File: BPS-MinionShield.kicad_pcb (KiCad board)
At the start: 2 copper layers, 85 x 66 mm, 81 parts, among them J1 TempConn1, J2 TempConn2, J3 Conn_01x24_Female

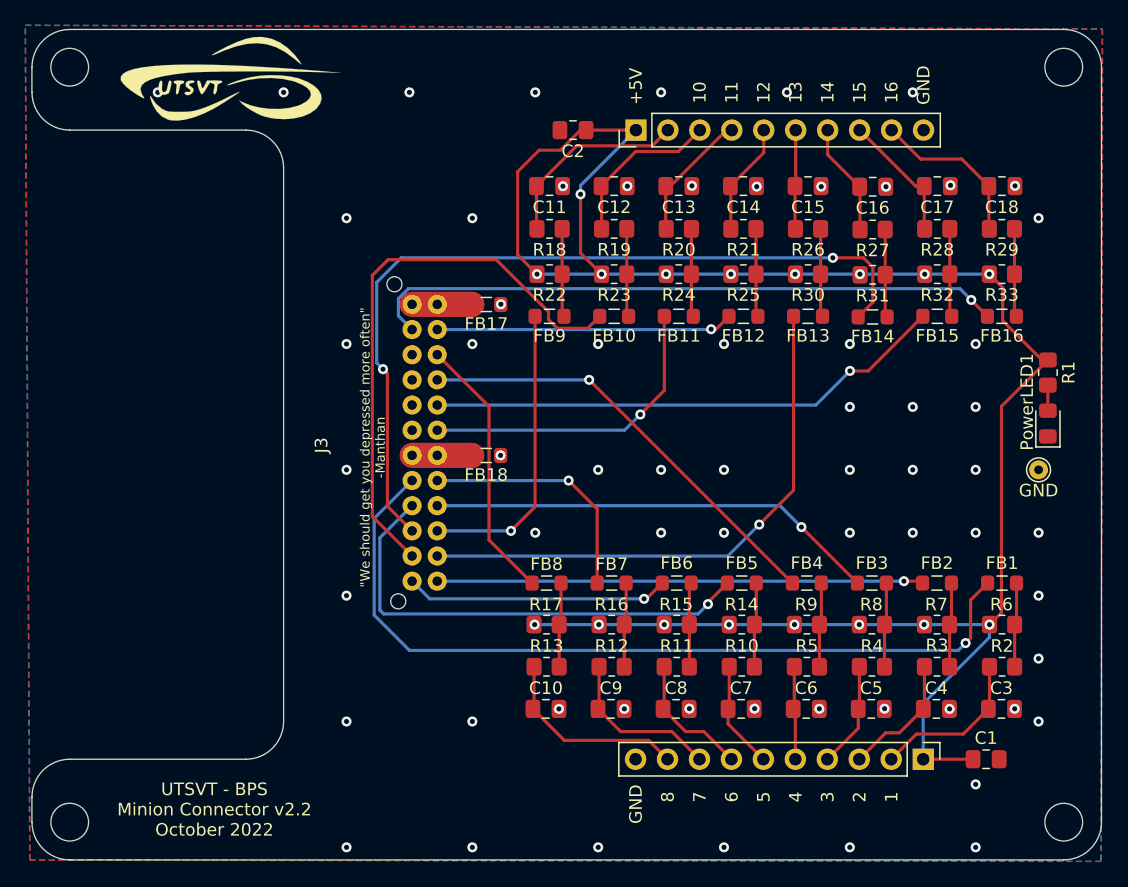
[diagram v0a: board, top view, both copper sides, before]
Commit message: move ferrite beads away from connector
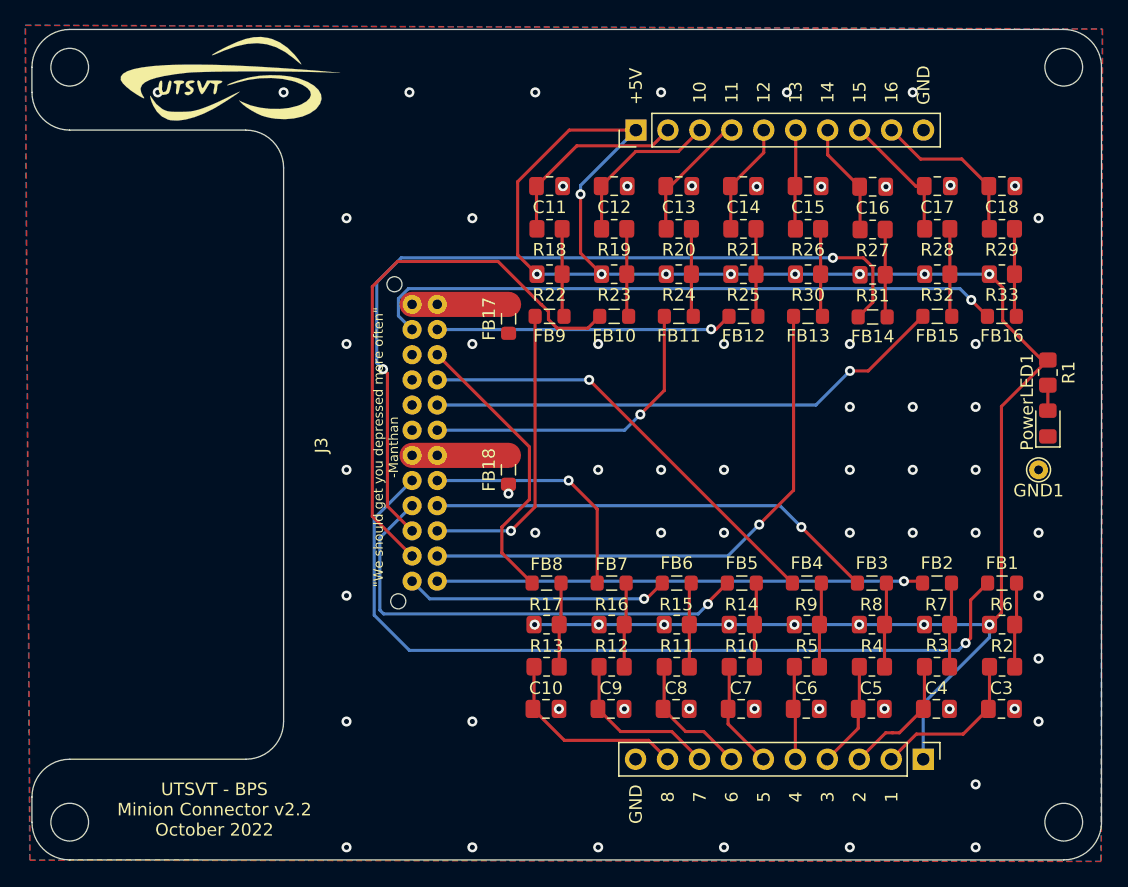
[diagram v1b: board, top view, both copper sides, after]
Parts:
- removed C1, C2: 1u, Capacitor_SMD:C_0805_2012Metric_Pad1.18x1.45mm_HandSolder
- moved FB18 2.11 mm to (137.9, 105.0), turned to 90 degrees
- moved FB17 2.11 mm to (137.9, 93.0), turned to 90 degrees
- renumbered GND to GND1
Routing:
- net +5V: track 154.4 -> 150.0 mm
- net Net-(FB18-Pad2): track 4.74 -> 7.66 mm
- net Net-(FB17-Pad2): track 4.75 -> 7.67 mm
- net /temp14: track 21.3 -> 23.1 mm
- net /temp7: track 45.2 -> 44.6 mm
- net GND: vias 64 -> 63

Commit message: fix some islands
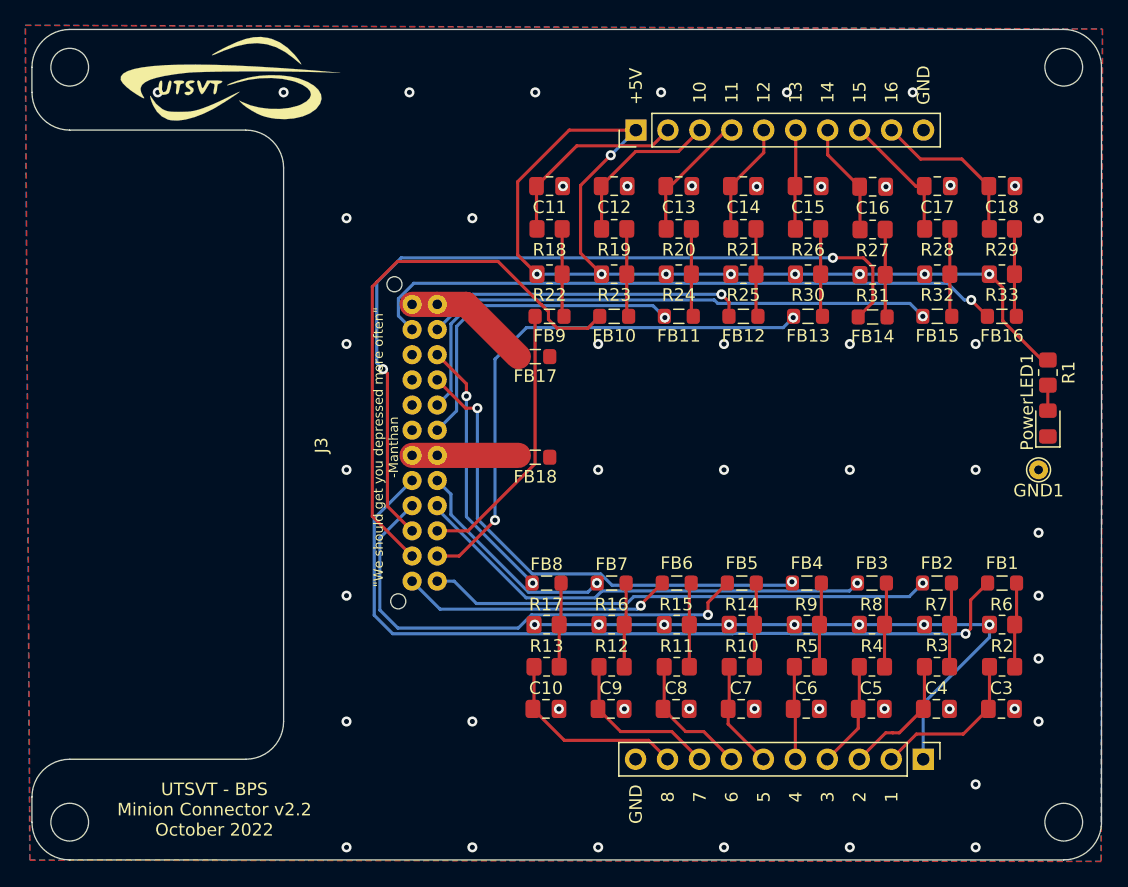
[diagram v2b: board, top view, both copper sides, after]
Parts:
- moved FB17 3.67 mm to (140.0, 96.0), turned to 180 degrees
- moved FB18 2.35 mm to (140.0, 104.0), turned to 180 degrees
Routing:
- net +5V: track 150.0 -> 127.1 mm
- net /temp13: track 34.9 -> 40.2 mm, vias 1 -> 2
- net /temp12: track 41.5 -> 45.7 mm
- net Net-(FB17-Pad2): track 7.67 -> 10.2 mm
- net /temp15: track 23.6 -> 25.7 mm
- net /temp3: track 23.7 -> 21.7 mm, vias 1 -> 0
- net /temp10: track 19.5 -> 17.6 mm
- net /temp14: track 23.1 -> 21.3 mm, vias 0 -> 2
- net /temp1: track 65.8 -> 64.3 mm
- net /temp2: track 38.2 -> 39.6 mm
- net /temp5: track 38.6 -> 40.0 mm
- net /temp11: track 25.2 -> 26.5 mm
- net /temp9: track 35.9 -> 37.1 mm
- net Net-(FB18-Pad2): track 7.66 -> 8.45 mm
- net /temp6: track 21.0 -> 21.7 mm
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
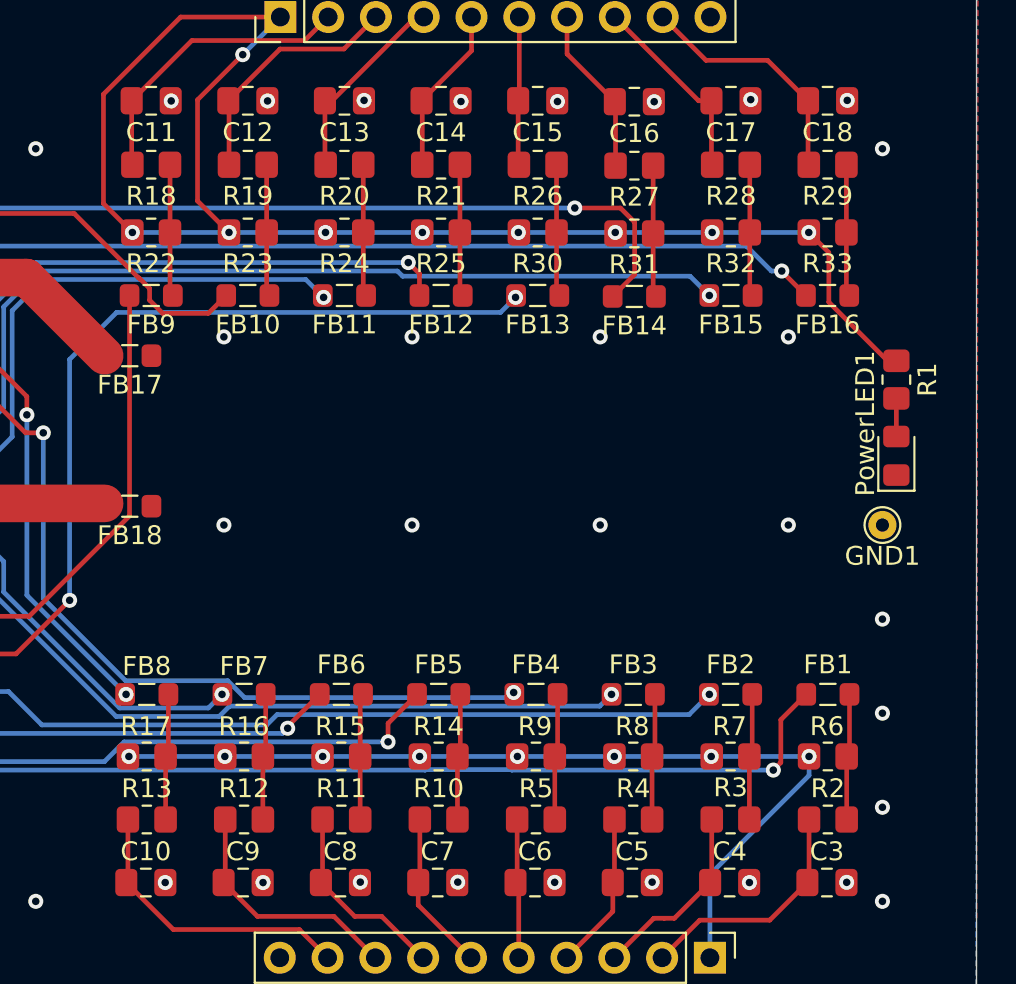
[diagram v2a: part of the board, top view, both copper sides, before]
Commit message: change cap values to 100nf
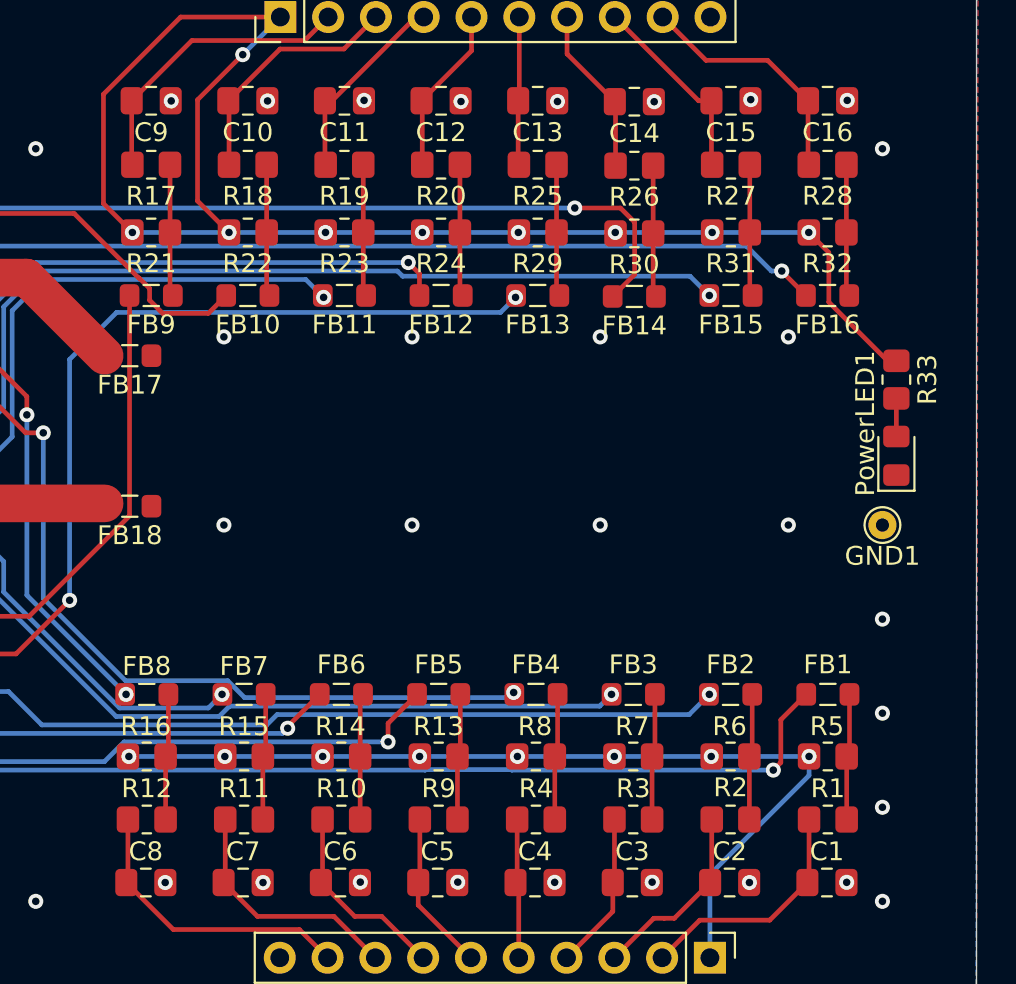
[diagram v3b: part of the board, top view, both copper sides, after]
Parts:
- C1: renamed from C3; value 1u -> 100nF
- C10: renamed from C12; value 1u -> 100nF
- C11: renamed from C13; value 1u -> 100nF
- C12: renamed from C14; value 1u -> 100nF
- C13: renamed from C15; value 1u -> 100nF
- C14: renamed from C16; value 1u -> 100nF
- C15: renamed from C17; value 1u -> 100nF
- C16: renamed from C18; value 1u -> 100nF
- C2: renamed from C4; value 1u -> 100nF
- C3: renamed from C5; value 1u -> 100nF
- C4: renamed from C6; value 1u -> 100nF
- C5: renamed from C7; value 1u -> 100nF
- C6: renamed from C8; value 1u -> 100nF
- C7: renamed from C9; value 1u -> 100nF
- C8: renamed from C10; value 1u -> 100nF
- C9: renamed from C11; value 1u -> 100nF
- renumbered R2 to R1, R11 to R10, R12 to R11, R13 to R12, R14 to R13, R15 to R14, R16 to R15, R17 to R16, R18 to R17, R19 to R18, R20 to R19, R3 to R2, R21 to R20, R22 to R21, R23 to R22, R24 to R23, R25 to R24, R26 to R25, R27 to R26, R28 to R27, R29 to R28, R30 to R29, R4 to R3, R31 to R30, R32 to R31, R33 to R32, R1 to R33, R5 to R4, R6 to R5, R7 to R6, R8 to R7, R9 to R8, R10 to R9

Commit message: address maestro tianda's review
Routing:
- net +5V: track 127.1 -> 112.8 mm, vias 17 -> 16
- net /temp1: track 64.3 -> 64.9 mm
- net /temp2: track 39.6 -> 39.1 mm
- net GND: vias 50 -> 39
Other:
- board text added: "9"

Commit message: address all tianda requests, start standardization
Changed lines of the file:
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@@
   (segment (start 152.407144 89.45) (end 152.407144 92.65) (width 0.25) (layer "F.Cu") (net 39))
   (segment (start 152.407144 85.85) (end 152.407144 89.45) (width 0.25) (layer "F.Cu") (net 39))
-  (via (at 150.3 92.9) (size 0.8) (drill 0.4) (layers "F.Cu" "B.Cu") (net 40))
-  (segment (start 133.747 93.603) (end 135.4 91.95) (width 0.25) (layer "B.Cu") (net 40))
-  (segment (start 132.21 101.85) (end 133.747 100.313) (width 0.25) (layer "B.Cu") (net 40))
-  (segment (start 149.35 91.95) (end 150.3 92.9) (width 0.25) (layer "B.Cu") (net 40))
-  (segment (start 135.4 91.95) (end 149.35 91.95) (width 0.25) (layer "B.Cu") (net 40))
-  (segment (start 133.747 100.313) (end 133.747 93.603) (width 0.25) (layer "B.Cu") (net 40))
+  (via (at 150.257144 92.8) (size 0.8) (drill 0.4) (layers "F.Cu" "B.Cu") (net 40))
+  (segment (start 149.407144 91.95) (end 135.4 91.95) (width 0.25) (layer "B.Cu") (net 40))
+  (segment (start 150.257144 92.8) (end 149.407144 91.95) (width 0.25) (layer "B.Cu") (net 40))
+  (segment (start 133.747 93.603) (end 133.747 100.313) (width 0.25) (layer "B.Cu") (net 40))
+  (segment (start 133.747 100.313) (end 132.21 101.85) (width 0.25) (layer "B.Cu") (net 40))
+  (segment (start 135.4 91.95) (end 133.747 93.603) (width 0.25) (layer "B.Cu") (net 40))
   (segment (start 157.542858 85.85) (end 157.542858 89.45) (width 0.25) (layer "F.Cu") (net 41))
   (segment (start 157.542858 92.65) (end 157.692858 92.8) (width 0.25) (layer "F.Cu") (net 41))
@@
   (segment (start 133.95 111.85) (end 132.21 111.85) (width 0.25) (layer "F.Cu") (net 44))
   (segment (start 136.8 109) (end 133.95 111.85) (width 0.25) (layer "F.Cu") (net 44))
-  (via (at 160.5 92.9) (size 0.8) (drill 0.4) (layers "F.Cu" "B.Cu") (net 44))
+  (via (at 160.528572 92.8) (size 0.8) (drill 0.4) (layers "F.Cu" "B.Cu") (net 44))
   (via (at 136.8 109) (size 0.8) (drill 0.4) (layers "F.Cu" "B.Cu") (net 44))
-  (segment (start 139.3 93.7) (end 159.7 93.7) (width 0.25) (layer "B.Cu") (net 44))
-  (segment (start 136.8 109) (end 136.8 96.2) (width 0.25) (layer "B.Cu") (net 44))
-  (segment (start 136.8 96.2) (end 139.3 93.7) (width 0.25) (layer "B.Cu") (net 44))
-  (segment (start 159.7 93.7) (end 160.5 92.9) (width 0.25) (layer "B.Cu") (net 44))
+  (segment (start 159.788572 93.54) (end 139.46 93.54) (width 0.25) (layer "B.Cu") (net 44))
+  (segment (start 136.8 96.2) (end 136.8 109) (width 0.25) (layer "B.Cu") (net 44))
+  (segment (start 160.528572 92.8) (end 159.788572 93.54) (width 0.25) (layer "B.Cu") (net 44))
+  (segment (start 139.46 93.54) (end 136.8 96.2) (width 0.25) (layer "B.Cu") (net 44))
   (segment (start 167.814286 85.9) (end 167.814286 89.5) (width 0.25) (layer "F.Cu") (net 45))
   (segment (start 167.814286 92.7) (end 167.964286 92.85) (width 0.25) (layer "F.Cu") (net 45))
   (segment (start 167.814286 89.5) (end 167.814286 92.7) (width 0.25) (layer "F.Cu") (net 45))
-  (segment (start 166.83 88.902541) (end 166.077459 88.15) (width 0.25) (layer "F.Cu") (net 46))
-  (segment (start 166.83 91.684286) (end 166.83 88.902541) (width 0.25) (layer "F.Cu") (net 46))
+  (segment (start 166.8 91.714286) (end 165.664286 92.85) (width 0.25) (layer "F.Cu") (net 46))
   (segment (start 128.25 107.89) (end 130.21 109.85) (width 0.25) (layer "F.Cu") (net 46))
-  (segment (start 166.077459 88.15) (end 163.65 88.15) (width 0.25) (layer "F.Cu") (net 46))
-  (segment (start 165.664286 92.85) (end 166.83 91.684286) (width 0.25) (layer "F.Cu") (net 46))
+  (segment (start 166.8 88.15) (end 166.8 91.714286) (width 0.25) (layer "F.Cu") (net 46))
   (segment (start 128.25 97.35) (end 128.25 107.89) (width 0.25) (layer "F.Cu") (net 46))
   (segment (start 127.9 97) (end 128.25 97.35) (width 0.25) (layer "F.Cu") (net 46))
   (via (at 127.9 97) (size 0.8) (drill 0.4) (layers "F.Cu" "B.Cu") (net 46))
-  (via (at 163.65 88.15) (size 0.8) (drill 0.4) (layers "F.Cu" "B.Cu") (net 46))
+  (via (at 166.8 88.15) (size 0.8) (drill 0.4) (layers "F.Cu" "B.Cu") (net 46))
+  (segment (start 129.35 88.15) (end 127.4 90.1) (width 0.25) (layer "B.Cu") (net 46))
   (segment (start 127.4 90.1) (end 127.4 96.5) (width 0.25) (layer "B.Cu") (net 46))
-  (segment (start 163.65 88.15) (end 129.35 88.15) (width 0.25) (layer "B.Cu") (net 46))
-  (segment (start 129.35 88.15) (end 127.4 90.1) (width 0.25) (layer "B.Cu") (net 46))
+  (segment (start 166.8 88.15) (end 129.35 88.15) (width 0.25) (layer "B.Cu") (net 46))
   (segment (start 127.4 96.5) (end 127.9 97) (width 0.25) (layer "B.Cu") (net 46))
   (segment (start 172.95 89.45) (end 172.95 92.65) (width 0.25) (layer "F.Cu") (net 47))
